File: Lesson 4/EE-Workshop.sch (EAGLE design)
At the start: 2 parts, among them U1 NE555N

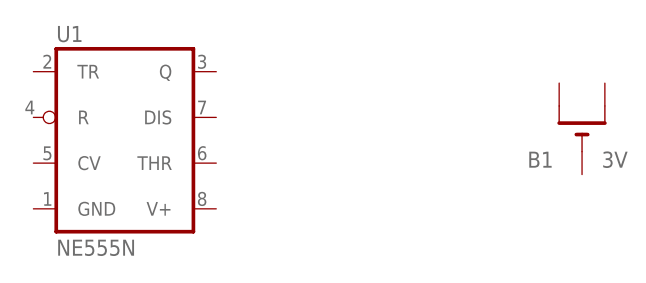
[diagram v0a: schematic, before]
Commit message: Updated Workshop Lesson 4
Extensive update to tutorials and schematics.
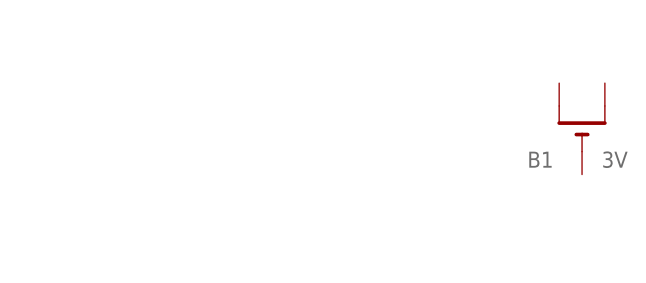
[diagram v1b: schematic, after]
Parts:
- removed U1: NE555N, linear:NE555N
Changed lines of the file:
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@@
 <attribute name="SPICEPREFIX" value="J"/>
-</part>
-<part name="U1" library="linear" library_urn="urn:adsk.eagle:library:262" deviceset="*555" device="N" package3d_urn="urn:adsk.eagle:package:16409/2" technology="NE">
-<attribute name="SPICEPREFIX" value="X"/>
 </part>
 </parts>
@@
 <attribute name="VALUE" x="46.99" y="52.07" size="1.778" layer="96" rot="R180"/>
 </instance>
-<instance part="U1" gate="A" x="-8.89" y="53.34" smashed="yes">
-<attribute name="NAME" x="-16.51" y="64.262" size="1.778" layer="95"/>
-<attribute name="VALUE" x="-16.51" y="40.513" size="1.778" layer="96"/>
-</instance>
 </instances>
